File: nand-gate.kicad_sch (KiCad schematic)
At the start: 3 parts, among them Q1 NPN, Q2 NPN

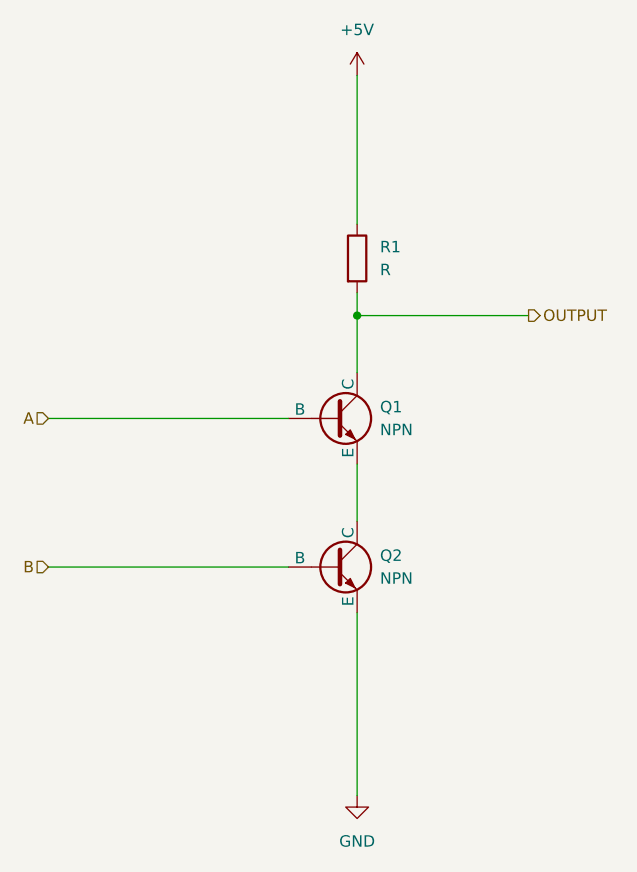
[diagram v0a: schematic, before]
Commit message: Create PCB layout
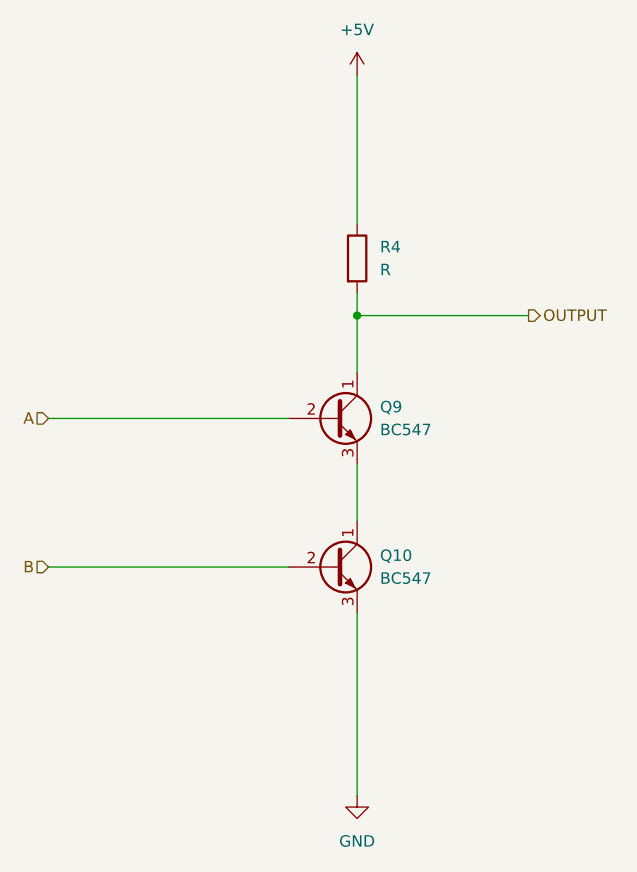
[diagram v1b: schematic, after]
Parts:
- removed Q1, Q2: NPN, symbol Simulation_SPICE:NPN
- added Q10, Q9: BC547, Package_TO_SOT_THT:TO-92_Inline, symbol Transistor_BJT:BC547
- R4: renamed from R1; footprint (none) -> Resistor_SMD:R_0201_0603Metric
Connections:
- net A: now also Q9.2 (B)
- net B: now also Q10.2 (B)
- net GND: now also Q10.3 (E)
- net OUTPUT: now also Q9.1 (C)
- new net: Q10.1 (C), Q9.3 (E)
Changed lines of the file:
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@@
   (symbol (lib_id "power:GND") (at 95.25 120.65 0) (unit 1)
     (in_bom yes) (on_board yes) (dnp no) (fields_autoplaced)
-    (property "Reference" "#PWR06" (at 95.25 127 0)
+    (property "Reference" "#PWR04" (at 95.25 127 0)
       (effects (font (size 1.27 1.27)) hide)
     )
@@
       (project "half-adder"
         (path "/88c27409-0a88-4cf1-8b65-cf7271709e32/29137efa-2cbb-4b26-94cf-0127fe654e5e/3c6c3515-201d-4b02-b79f-e9c4c0dfa7c4"
-          (reference "#PWR06") (unit 1)
+          (reference "#PWR04") (unit 1)
         )
         (path "/88c27409-0a88-4cf1-8b65-cf7271709e32/dbe7fac6-3d6a-4481-b9c3-f6b25e3c84ad/3c6c3515-201d-4b02-b79f-e9c4c0dfa7c4"
-          (reference "#PWR03") (unit 1)
+          (reference "#PWR08") (unit 1)
         )
       )
@@
   (symbol (lib_id "power:+5V") (at 95.25 40.64 0) (unit 1)
     (in_bom yes) (on_board yes) (dnp no) (fields_autoplaced)
-    (property "Reference" "#PWR05" (at 95.25 44.45 0)
+    (property "Reference" "#PWR03" (at 95.25 44.45 0)
       (effects (font (size 1.27 1.27)) hide)
     )
@@
       (project "half-adder"
         (path "/88c27409-0a88-4cf1-8b65-cf7271709e32/29137efa-2cbb-4b26-94cf-0127fe654e5e/3c6c3515-201d-4b02-b79f-e9c4c0dfa7c4"
-          (reference "#PWR05") (unit 1)
+          (reference "#PWR03") (unit 1)
         )
         (path "/88c27409-0a88-4cf1-8b65-cf7271709e32/dbe7fac6-3d6a-4481-b9c3-f6b25e3c84ad/3c6c3515-201d-4b02-b79f-e9c4c0dfa7c4"
-          (reference "#PWR01") (unit 1)
+          (reference "#PWR07") (unit 1)
         )
       )
@@
   (symbol (lib_id "Device:R") (at 95.25 60.96 0) (unit 1)
     (in_bom yes) (on_board yes) (dnp no) (fields_autoplaced)
-    (property "Reference" "R1" (at 97.79 59.69 0)
+    (property "Reference" "R4" (at 97.79 59.69 0)
       (effects (font (size 1.27 1.27)) (justify left))
     )
@@
       (effects (font (size 1.27 1.27)) (justify left))
     )
-    (property "Footprint" "" (at 93.472 60.96 90)
+    (property "Footprint" "Resistor_SMD:R_0201_0603Metric" (at 93.472 60.96 90)
       (effects (font (size 1.27 1.27)) hide)
     )
@@
       (project "half-adder"
         (path "/88c27409-0a88-4cf1-8b65-cf7271709e32/29137efa-2cbb-4b26-94cf-0127fe654e5e/3c6c3515-201d-4b02-b79f-e9c4c0dfa7c4"
-          (reference "R1") (unit 1)
+          (reference "R4") (unit 1)
         )
         (path "/88c27409-0a88-4cf1-8b65-cf7271709e32/dbe7fac6-3d6a-4481-b9c3-f6b25e3c84ad/3c6c3515-201d-4b02-b79f-e9c4c0dfa7c4"
-          (reference "R4") (unit 1)
+          (reference "R8") (unit 1)
         )
       )
     )
   )
-  (symbol (lib_id "Simulation_SPICE:NPN") (at 92.71 78.74 0) (unit 1)
+  (symbol (lib_id "Transistor_BJT:BC547") (at 92.71 95.25 0) (unit 1)
     (in_bom yes) (on_board yes) (dnp no) (fields_autoplaced)
-    (property "Reference" "Q1" (at 97.79 77.47 0)
+    (property "Reference" "Q10" (at 97.79 93.98 0)
       (effects (font (size 1.27 1.27)) (justify left))
     )
-    (property "Value" "NPN" (at 97.79 80.01 0)
+    (property "Value" "BC547" (at 97.79 96.52 0)
       (effects (font (size 1.27 1.27)) (justify left))
     )
-    (property "Footprint" "" (at 156.21 78.74 0)
-      (effects (font (size 1.27 1.27)) hide)
+    (property "Footprint" "Package_TO_SOT_THT:TO-92_Inline" (at 97.79 97.155 0)
+      (effects (font (size 1.27 1.27) italic) (justify left) hide)
     )
-    (property "Datasheet" "~" (at 156.21 78.74 0)
-      (effects (font (size 1.27 1.27)) hide)
-    )
-    (property "Sim.Device" "NPN" (at 92.71 78.74 0)
-      (effects (font (size 1.27 1.27)) hide)
-    )
-    (property "Sim.Type" "GUMMELPOON" (at 92.71 78.74 0)
-      (effects (font (size 1.27 1.27)) hide)
-    )
-    (property "Sim.Pins" "1=C 2=B 3=E" (at 92.71 78.74 0)
-      (effects (font (size 1.27 1.27)) hide)
+    (property "Datasheet" "https://www.onsemi.com/pub/Collateral/BC550-D.pdf" (at 92.71 95.25 0)
+      (effects (font (size 1.27 1.27)) (justify left) hide)
     )
     (pin "1")
@@
     (instances
       (project "half-adder"
+        (path "/88c27409-0a88-4cf1-8b65-cf7271709e32/dbe7fac6-3d6a-4481-b9c3-f6b25e3c84ad/3c6c3515-201d-4b02-b79f-e9c4c0dfa7c4"
+          (reference "Q10") (unit 1)
+        )
         (path "/88c27409-0a88-4cf1-8b65-cf7271709e32/29137efa-2cbb-4b26-94cf-0127fe654e5e/3c6c3515-201d-4b02-b79f-e9c4c0dfa7c4"
-          (reference "Q1") (unit 1)
-        )
-        (path "/88c27409-0a88-4cf1-8b65-cf7271709e32/dbe7fac6-3d6a-4481-b9c3-f6b25e3c84ad/3c6c3515-201d-4b02-b79f-e9c4c0dfa7c4"
-          (reference "Q4") (unit 1)
+          (reference "Q5") (unit 1)
         )
       )
     )
   )
-  (symbol (lib_id "Simulation_SPICE:NPN") (at 92.71 95.25 0) (unit 1)
+  (symbol (lib_id "Transistor_BJT:BC547") (at 92.71 78.74 0) (unit 1)
     (in_bom yes) (on_board yes) (dnp no) (fields_autoplaced)
-    (property "Reference" "Q2" (at 97.79 93.98 0)
+    (property "Reference" "Q9" (at 97.79 77.47 0)
       (effects (font (size 1.27 1.27)) (justify left))
     )
-    (property "Value" "NPN" (at 97.79 96.52 0)
+    (property "Value" "BC547" (at 97.79 80.01 0)
       (effects (font (size 1.27 1.27)) (justify left))
     )
-    (property "Footprint" "" (at 156.21 95.25 0)
-      (effects (font (size 1.27 1.27)) hide)
+    (property "Footprint" "Package_TO_SOT_THT:TO-92_Inline" (at 97.79 80.645 0)
+      (effects (font (size 1.27 1.27) italic) (justify left) hide)
     )
-    (property "Datasheet" "~" (at 156.21 95.25 0)
-      (effects (font (size 1.27 1.27)) hide)
-    )
-    (property "Sim.Device" "NPN" (at 92.71 95.25 0)
-      (effects (font (size 1.27 1.27)) hide)
-    )
-    (property "Sim.Type" "GUMMELPOON" (at 92.71 95.25 0)
-      (effects (font (size 1.27 1.27)) hide)
-    )
-    (property "Sim.Pins" "1=C 2=B 3=E" (at 92.71 95.25 0)
-      (effects (font (size 1.27 1.27)) hide)
+    (property "Datasheet" "https://www.onsemi.com/pub/Collateral/BC550-D.pdf" (at 92.71 78.74 0)
+      (effects (font (size 1.27 1.27)) (justify left) hide)
     )
     (pin "1")
@@
     (instances
       (project "half-adder"
+        (path "/88c27409-0a88-4cf1-8b65-cf7271709e32/dbe7fac6-3d6a-4481-b9c3-f6b25e3c84ad/3c6c3515-201d-4b02-b79f-e9c4c0dfa7c4"
+          (reference "Q9") (unit 1)
+        )
         (path "/88c27409-0a88-4cf1-8b65-cf7271709e32/29137efa-2cbb-4b26-94cf-0127fe654e5e/3c6c3515-201d-4b02-b79f-e9c4c0dfa7c4"
-          (reference "Q2") (unit 1)
-        )
-        (path "/88c27409-0a88-4cf1-8b65-cf7271709e32/dbe7fac6-3d6a-4481-b9c3-f6b25e3c84ad/3c6c3515-201d-4b02-b79f-e9c4c0dfa7c4"
-          (reference "Q5") (unit 1)
+          (reference "Q4") (unit 1)
         )
       )
